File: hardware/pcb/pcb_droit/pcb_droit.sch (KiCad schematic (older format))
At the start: 19 parts, among them P1 TE-FFC-10-0.5

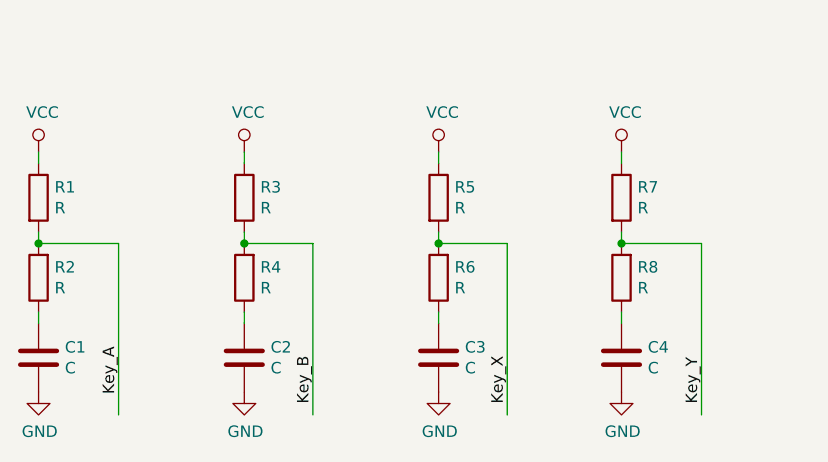
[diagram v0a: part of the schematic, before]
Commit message: Modifications des fonts et debut de la creation du drivers de touches
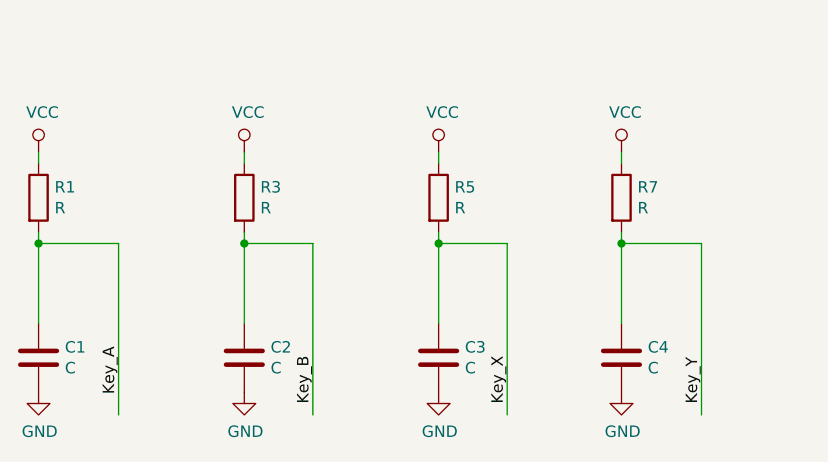
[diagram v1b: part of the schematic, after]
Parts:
- removed R2, R4, R6, R8: R, Resistor_SMD:R_1206_3216Metric_Pad1.42x1.75mm_HandSolder, symbol Device:R
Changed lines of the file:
@@
 EESchema Schematic File Version 4
+LIBS:pcb_droit-cache
 EELAYER 26 0
 EELAYER END
@@
 $EndComp
 $Comp
-L Device:R R2
-U 1 1 5C793610
-P 1950 5750
-F 0 "R2" H 1880 5704 50  0000 R CNN
-F 1 "R" H 1880 5795 50  0000 R CNN
-F 2 "Resistor_SMD:R_1206_3216Metric_Pad1.42x1.75mm_HandSolder" V 1880 5750 50  0001 C CNN
-F 3 "~" H 1950 5750 50  0001 C CNN
-	1    1950 5750
-	-1   0    0    1
-$EndComp
-$Comp
 L power:GND #PWR0103
 U 1 1 5C7938F7
@@
 $EndComp
 Wire Wire Line
-	1950 5900 1950 5950
-Wire Wire Line
 	1950 5550 1950 5600
 $Comp
@@
 $EndComp
 $Comp
-L Device:R R4
-U 1 1 5C795C8C
-P 2850 5750
-F 0 "R4" H 2780 5704 50  0000 R CNN
-F 1 "R" H 2780 5795 50  0000 R CNN
-F 2 "Resistor_SMD:R_1206_3216Metric_Pad1.42x1.75mm_HandSolder" V 2780 5750 50  0001 C CNN
-F 3 "~" H 2850 5750 50  0001 C CNN
-	1    2850 5750
-	-1   0    0    1
-$EndComp
-$Comp
 L power:GND #PWR0105
 U 1 1 5C795C93
@@
 $EndComp
 Wire Wire Line
-	2850 5900 2850 5950
-Wire Wire Line
 	2850 5550 2850 5600
 $Comp
@@
 $EndComp
 $Comp
-L Device:R R6
-U 1 1 5C79623C
-P 3700 5750
-F 0 "R6" H 3630 5704 50  0000 R CNN
-F 1 "R" H 3630 5795 50  0000 R CNN
-F 2 "Resistor_SMD:R_1206_3216Metric_Pad1.42x1.75mm_HandSolder" V 3630 5750 50  0001 C CNN
-F 3 "~" H 3700 5750 50  0001 C CNN
-	1    3700 5750
-	-1   0    0    1
-$EndComp
-$Comp
 L power:GND #PWR0107
 U 1 1 5C796243
@@
 $EndComp
 Wire Wire Line
-	3700 5900 3700 5950
-Wire Wire Line
 	3700 5550 3700 5600
 $Comp
@@
 $EndComp
 $Comp
-L Device:R R8
-U 1 1 5C79684A
-P 4500 5750
-F 0 "R8" H 4430 5704 50  0000 R CNN
-F 1 "R" H 4430 5795 50  0000 R CNN
-F 2 "Resistor_SMD:R_1206_3216Metric_Pad1.42x1.75mm_HandSolder" V 4430 5750 50  0001 C CNN
-F 3 "~" H 4500 5750 50  0001 C CNN
-	1    4500 5750
-	-1   0    0    1
-$EndComp
-$Comp
 L power:GND #PWR0109
 U 1 1 5C796851
@@
 	1    0    0    -1
 $EndComp
-Wire Wire Line
-	4500 5900 4500 5950
 Wire Wire Line
 	4500 5550 4500 5600
@@
 Wire Wire Line
 	2300 5600 2300 6350
-Connection ~ 1950 5600
 Wire Wire Line
 	2850 5600 3150 5600
 Wire Wire Line
 	3150 5600 3150 6350
-Connection ~ 2850 5600
 Wire Wire Line
 	3700 5600 4000 5600
 Wire Wire Line
 	4000 5600 4000 6350
-Connection ~ 3700 5600
 Wire Wire Line
 	4500 5600 4850 5600
 Wire Wire Line
 	4850 5600 4850 6350
-Connection ~ 4500 5600
 Text Label 2300 6050 3    50   ~ 0
 Key_A
@@
 Text Label 3950 1350 0    50   ~ 0
 Key_Rst
+Wire Wire Line
+	4500 5600 4500 5950
+Connection ~ 4500 5600
+Wire Wire Line
+	3700 5600 3700 5950
+Connection ~ 3700 5600
+Wire Wire Line
+	2850 5600 2850 5950
+Connection ~ 2850 5600
+Wire Wire Line
+	1950 5600 1950 5950
+Connection ~ 1950 5600
 $EndSCHEMATC

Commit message: ajout du wifi (debut) et mise a jour pcb
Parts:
- SW_A1: footprint Button_Switch_THT:SW_PUSH_6mm -> Insa:RubberKey
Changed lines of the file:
@@
-$EndComp
-$Comp
-L Switch:SW_Push SW_A1
-U 1 1 5C77EAF2
-P 3050 1750
-F 0 "SW_A1" H 3050 2035 50  0000 C CNN
-F 1 "SW_Push" H 3050 1944 50  0000 C CNN
-F 2 "Button_Switch_THT:SW_PUSH_6mm" H 3050 1950 50  0001 C CNN
-F 3 "~" H 3050 1950 50  0001 C CNN
-	1    3050 1750
-	1    0    0    -1
 $EndComp
 $Comp
@@
 	1950 5600 1950 5950
 Connection ~ 1950 5600
+$Comp
+L Switch:SW_Push SW_A1
+U 1 1 5CB760F5
+P 3050 1750
+F 0 "SW_A1" H 3050 2035 50  0000 C CNN
+F 1 "SW_Push" H 3050 1944 50  0000 C CNN
+F 2 "Insa:RubberKey" H 3050 1950 50  0001 C CNN
+F 3 "~" H 3050 1950 50  0001 C CNN
+	1    3050 1750
+	1    0    0    -1
+$EndComp
 $EndSCHEMATC

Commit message: mise a jour des pcb et design mecaniques
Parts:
- added Logo1: LOGO, Insa:insa-image, symbol insa-sym:LOGO
- SW_A1: footprint Insa:RubberKey -> Insa:RubberKey-4mm-2
- SW_B1, SW_X1, SW_Y1: footprint Button_Switch_THT:SW_PUSH_6mm -> Insa:RubberKey-4mm-2
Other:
- note added: "INSA Toulouse"
- note added: "PCB keys right"
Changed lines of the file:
@@
 F 0 "SW_Y1" H 3650 2435 50  0000 C CNN
 F 1 "SW_Push" H 3650 2344 50  0000 C CNN
-F 2 "Button_Switch_THT:SW_PUSH_6mm" H 3650 2350 50  0001 C CNN
+F 2 "Insa:RubberKey-4mm-2" H 3650 2350 50  0001 C CNN
 F 3 "~" H 3650 2350 50  0001 C CNN
 	1    3650 2150
@@
 F 0 "SW_B1" H 2600 2435 50  0000 C CNN
 F 1 "SW_Push" H 2600 2344 50  0000 C CNN
-F 2 "Button_Switch_THT:SW_PUSH_6mm" H 2600 2350 50  0001 C CNN
+F 2 "Insa:RubberKey-4mm-2" H 2600 2350 50  0001 C CNN
 F 3 "~" H 2600 2350 50  0001 C CNN
 	1    2600 2150
@@
 F 0 "SW_X1" H 3050 2835 50  0000 C CNN
 F 1 "SW_Push" H 3050 2744 50  0000 C CNN
-F 2 "Button_Switch_THT:SW_PUSH_6mm" H 3050 2750 50  0001 C CNN
+F 2 "Insa:RubberKey-4mm-2" H 3050 2750 50  0001 C CNN
 F 3 "~" H 3050 2750 50  0001 C CNN
 	1    3050 2550
@@
 F 0 "SW_A1" H 3050 2035 50  0000 C CNN
 F 1 "SW_Push" H 3050 1944 50  0000 C CNN
-F 2 "Insa:RubberKey" H 3050 1950 50  0001 C CNN
+F 2 "Insa:RubberKey-4mm-2" H 3050 1950 50  0001 C CNN
 F 3 "~" H 3050 1950 50  0001 C CNN
 	1    3050 1750
 	1    0    0    -1
 $EndComp
+$Comp
+L insa-sym:LOGO Logo1
+U 1 1 5CC05C32
+P 7700 6850
+F 0 "Logo1" H 7700 6398 60  0001 C CNN
+F 1 "LOGO" H 7700 7302 60  0001 C CNN
+F 2 "Insa:insa-image" H 7700 6850 50  0001 C CNN
+F 3 "" H 7700 6850 50  0001 C CNN
+	1    7700 6850
+	1    0    0    -1
+$EndComp
+Text Notes 8400 6800 0    118  ~ 24
+INSA Toulouse
+Text Notes 7400 7500 0    79   ~ 16
+PCB keys right
 $EndSCHEMATC
